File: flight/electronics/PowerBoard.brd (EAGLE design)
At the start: 80 x 80 mm, 13 parts, among them X1 JST-XH-02-PIN, X2 JST-XH-03-PIN, X3 JST-XH-03-PIN, X4 JST-XH-02-PIN, X6 JST-XH-03-PIN

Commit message: rev1 changes
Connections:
- net SWO: now also X2.PIN3, X3.PIN3, X4.PIN2, X6.PIN3
- net VBAT: no longer X2.PIN3, X3.PIN3, X4.PIN2, X6.PIN3
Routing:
- net SWO: track 73.7 -> 160.3 mm
- net VBAT: track 147.2 -> 82.8 mm
- net 3V3: track 106.8 -> 96.6 mm, vias 1 -> 0
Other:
- board text added: "KAOS-1 POWER BOWRD REV1"
- board text removed: "EXTRA"
- board text removed: "KAOS 1 POWER BOWRD REV1"
- board text removed: "SENS"

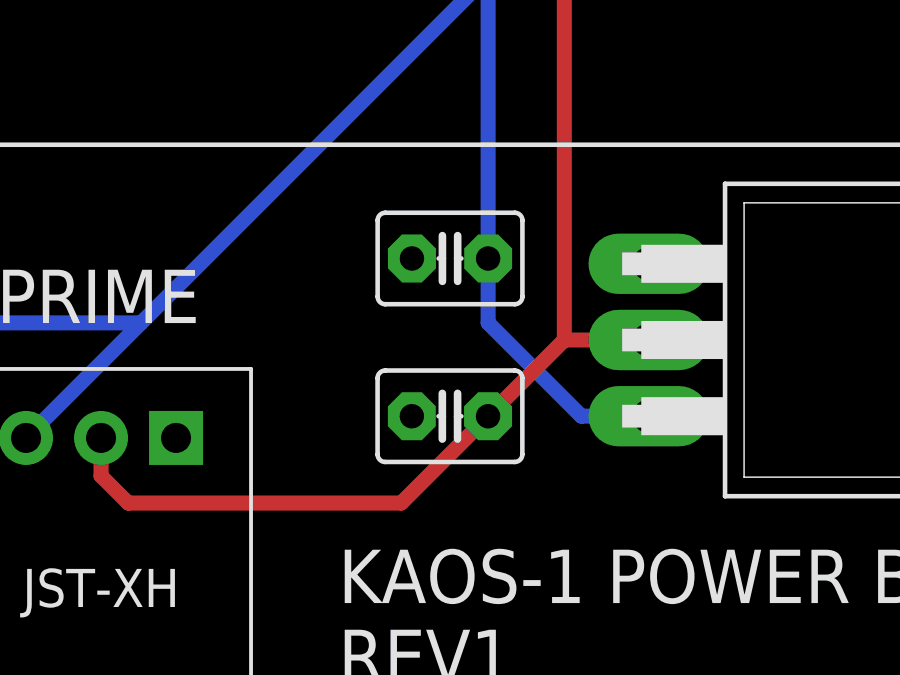
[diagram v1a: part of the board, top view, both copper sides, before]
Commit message: update caps on pb
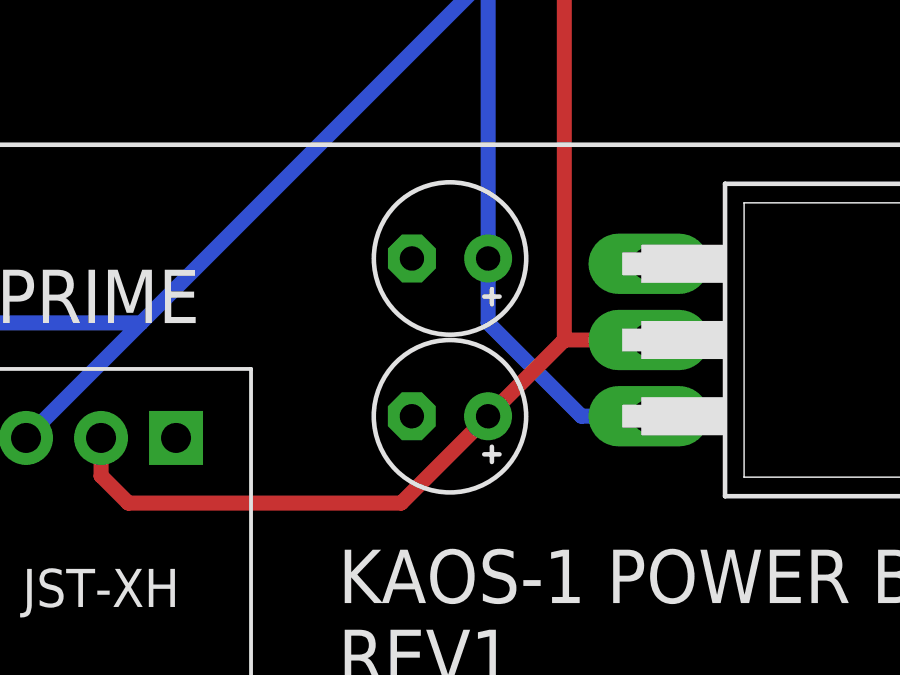
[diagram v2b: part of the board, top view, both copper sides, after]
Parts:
- C1, C2: device capacitor-wima:C2.5-3 -> rcl:E2,5-5
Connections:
- net 3V3: now also C2.+; no longer C2.1
- net GND: now also C1.-, C2.-; no longer C1.2, C2.2
- net SWO: now also C1.+; no longer C1.1
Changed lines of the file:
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@@
 <attribute name="MFR_NAME" value="Keystone Electronics" x="103" y="1.25" size="1.778" layer="21" display="off"/>
 </element>
-<element name="C1" library="capacitor-wima" library_urn="urn:adsk.eagle:library:116" package="C2.5-3" package3d_urn="urn:adsk.eagle:package:5436/1" value="33uF" x="36.72538125" y="16.152934375" smashed="yes" rot="R180">
-<attribute name="POPULARITY" value="38" x="10.05538125" y="111.402934375" size="1.778" layer="27" rot="R180" display="off"/>
-<attribute name="VALUE" x="33.557534375" y="12.98461875" size="1.27" layer="27" ratio="10"/>
+<element name="C1" library="rcl" library_urn="urn:adsk.eagle:library:334" package="E2,5-5" package3d_urn="urn:adsk.eagle:package:23344/1" value="33uF" x="36.72538125" y="16.152934375" smashed="yes" rot="R180">
+<attribute name="POPULARITY" value="8" x="10.05538125" y="111.402934375" size="1.778" layer="27" rot="R180" display="off"/>
+<attribute name="SPICEPREFIX" value="C" x="36.72538125" y="16.152934375" size="1.778" layer="27" rot="R180" display="off"/>
 </element>
-<element name="C2" library="capacitor-wima" library_urn="urn:adsk.eagle:library:116" package="C2.5-3" package3d_urn="urn:adsk.eagle:package:5436/1" value="0.47uF" x="36.723059375" y="10.894296875" smashed="yes" rot="R180">
-<attribute name="POPULARITY" value="38" x="3.703059375" y="106.144296875" size="1.778" layer="27" rot="R180" display="off"/>
-<attribute name="VALUE" x="39.06585" y="8.97311875" size="1.27" layer="27" ratio="10" rot="R180"/>
+<element name="C2" library="rcl" library_urn="urn:adsk.eagle:library:334" package="E2,5-5" package3d_urn="urn:adsk.eagle:package:23344/1" value="0.47uF" x="36.723059375" y="10.894296875" smashed="yes" rot="R180">
+<attribute name="POPULARITY" value="8" x="3.703059375" y="106.144296875" size="1.778" layer="27" rot="R180" display="off"/>
+<attribute name="SPICEPREFIX" value="C" x="36.723059375" y="10.894296875" size="1.778" layer="27" rot="R180" display="off"/>
 </element>
 <element name="X1" library="JST-XH Connectors" package="JST-XH_S2B" value="JST-XH-02-PIN" x="64.9590375" y="69.852475" locked="yes" smashed="yes"/>
@@
 <signals>
 <signal name="GND">
-<contactref element="C1" pad="2"/>
-<contactref element="C2" pad="2"/>
+<contactref element="C1" pad="-"/>
+<contactref element="C2" pad="-"/>
 <contactref element="X4" pad="PIN1"/>
 <contactref element="X2" pad="PIN1"/>
@@
 <signal name="SWO">
 <contactref element="X1" pad="PIN1"/>
-<contactref element="C1" pad="1"/>
+<contactref element="C1" pad="+"/>
 <contactref element="U$1" pad="3"/>
 <wire x1="43.3523125" y1="10.895725" x2="41.104275" y2="10.895725" width="0.5" layer="16"/>
@@
 <contactref element="X3" pad="PIN2"/>
 <contactref element="X6" pad="PIN2"/>
-<contactref element="C2" pad="1"/>
+<contactref element="C2" pad="+"/>
 <contactref element="U$1" pad="2"/>
 <wire x1="40.5344875" y1="13.435725" x2="37.993059375" y2="10.894296875" width="0.5" layer="1"/>
